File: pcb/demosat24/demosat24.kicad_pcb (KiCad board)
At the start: 2 copper layers, 68.6 x 53.3 mm, 28 parts, among them J1 Power, J10 Conn_01x03, J11 Conn_01x02, J12 Conn_01x02, J13 Conn_01x03, J2 Digital/PWM, J3 Analog, J4 Digital/PWM, J5 Conn_01x04, J6 Conn_01x04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

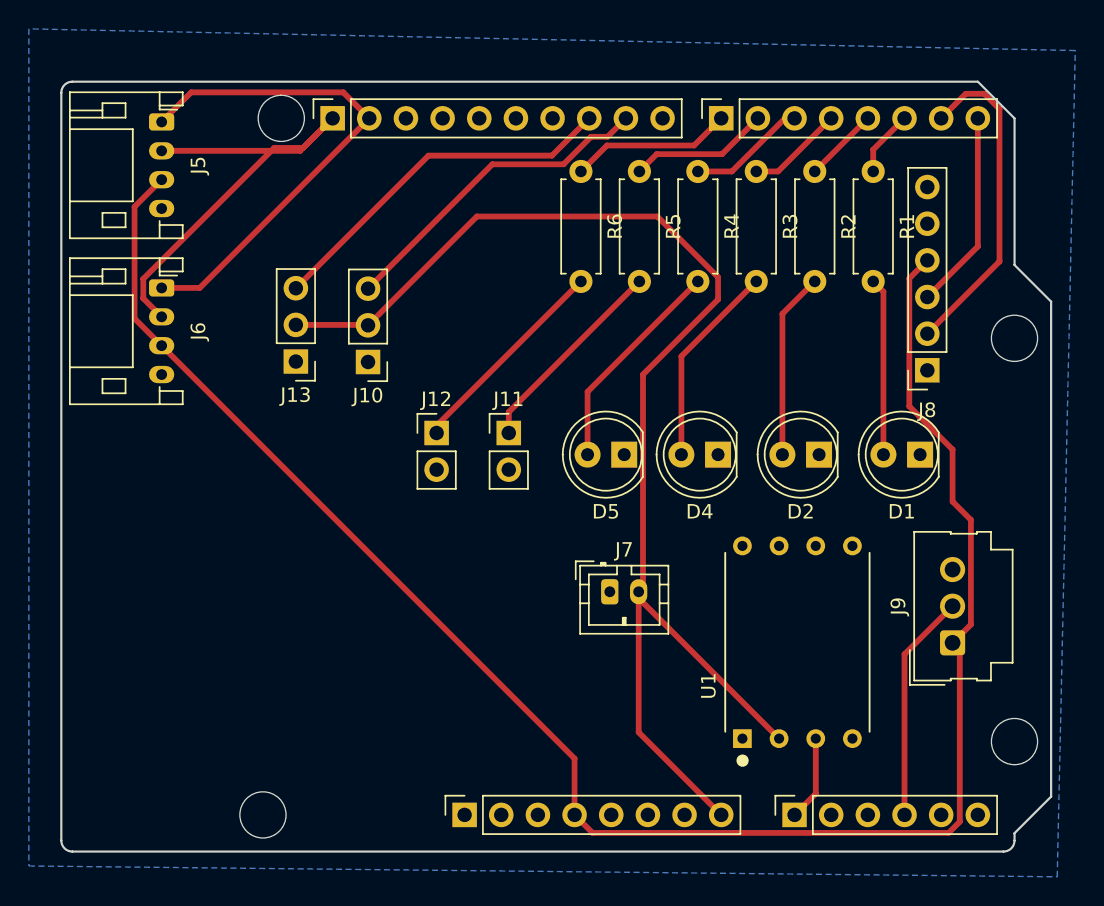
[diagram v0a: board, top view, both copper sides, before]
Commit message: updated pcb design with information learned from assembling the board
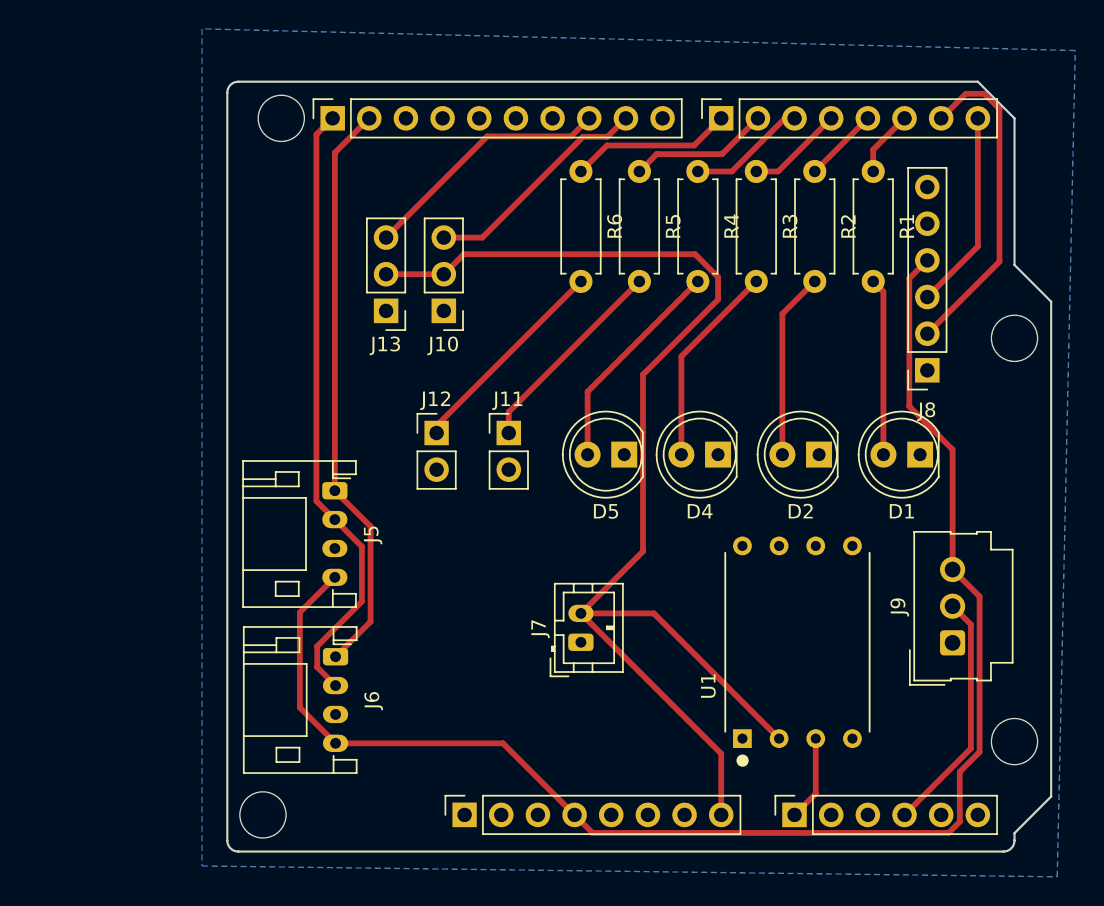
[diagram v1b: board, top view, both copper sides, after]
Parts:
- moved J6 28.2 mm to (119.0, 86.5)
- moved J5 28.2 mm to (119.0, 75.0)
- moved J13 7.17 mm to (122.5, 62.5)
- moved J10 6.33 mm to (126.5, 62.5)
- moved J7 4.03 mm to (136.0, 85.5), turned to 90 degrees
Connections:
- J5 pad 3: +3V3 -> GND
- J5 pad 4: GND -> +3V3
- J6 pad 3: +3V3 -> GND
- J6 pad 4: GND -> +3V3
- J9 pad 1: +3V3 -> GND
- J9 pad 3: GND -> +3V3
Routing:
- net +3V3: track 126.2 -> 101.7 mm
- net /SCL/A5: track 33.7 -> 42.9 mm
- net /*10: track 25.2 -> 17.5 mm
- net /*9: track 22.8 -> 16.0 mm
- net /SDA/A4: track 35.2 -> 40.3 mm
- net VCC: track 89.5 -> 86.8 mm
- net /A3: track 15.8 -> 16.9 mm
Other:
- board size 68.6 x 53.3 mm -> 57.1 x 53.3 mm
